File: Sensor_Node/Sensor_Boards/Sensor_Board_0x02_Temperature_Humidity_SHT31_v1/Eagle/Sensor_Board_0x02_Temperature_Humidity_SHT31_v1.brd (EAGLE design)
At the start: 55 x 35 mm, 15 parts, among them J1 M04_SMD_90, J2 M07_SMD_STRAIGHT, J4 ARDUINO_ISP, U2 ATMEGA328P_TQFP, Y1 8MHZ

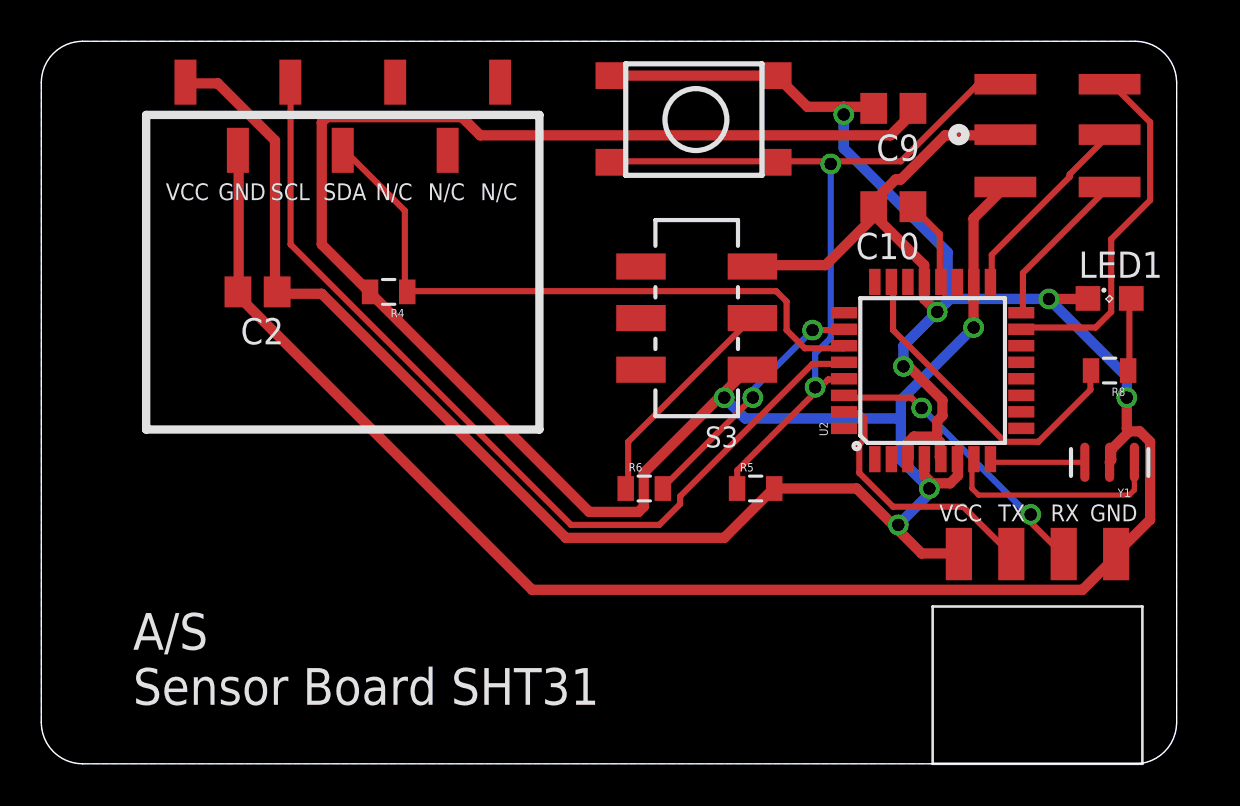
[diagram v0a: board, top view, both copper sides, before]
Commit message: Changes on SensModule SHT31
- removed R4
- added pogopin programming connector
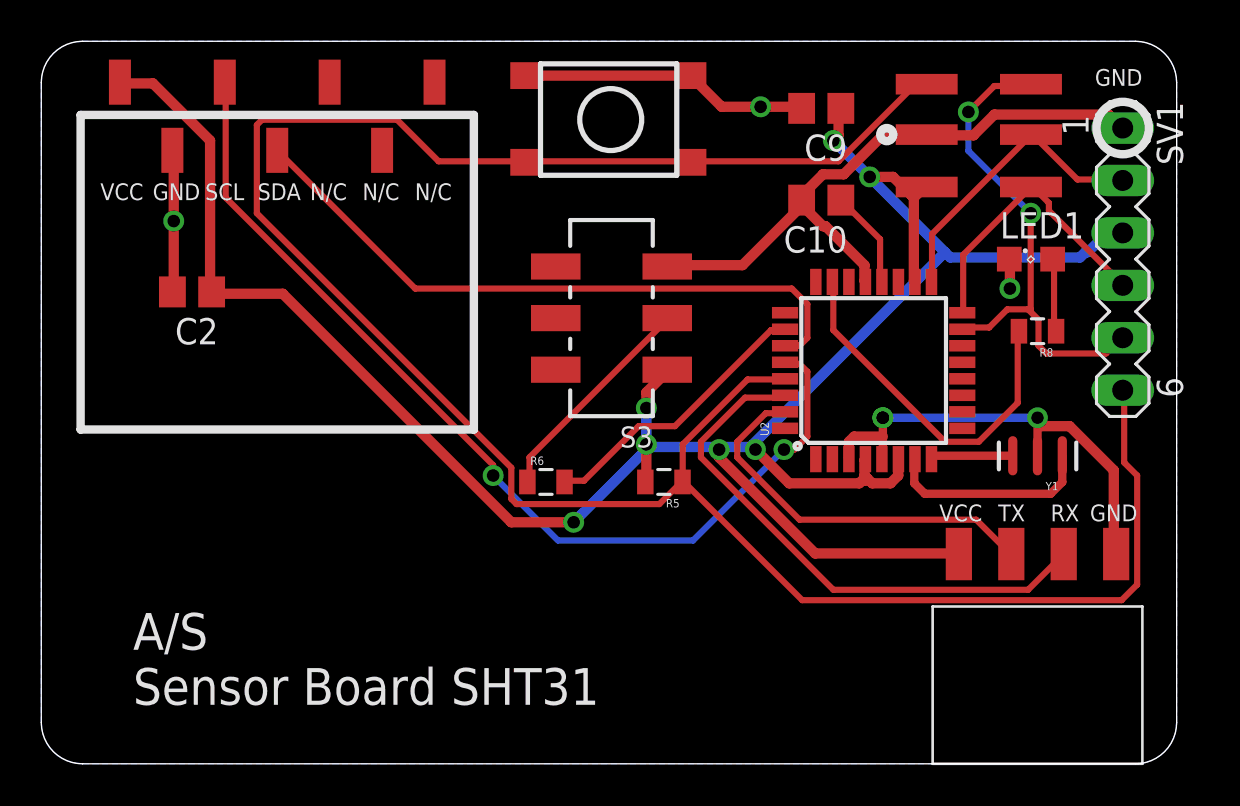
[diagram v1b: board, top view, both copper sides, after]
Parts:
- removed R4: 10k, SparkFun-Passives:0805
- added SV1: (no value), con-lstb:MA06-1
- moved R6 4.77 mm to (24.4, 13.7)
- moved R5 4.46 mm to (30.2, 13.7), turned to 180 degrees
- moved LED1 4.26 mm to (47.9, 24.4)
- moved S3 4.13 mm to (27.6, 21.6)
- moved S1 4.13 mm to (23.5, 33.3)
- moved R8 3.98 mm to (48.3, 21.0)
- moved J4 3.81 mm to (47.9, 27.9)
- moved C10 3.51 mm to (37.8, 27.3)
- moved Y1 3.51 mm to (48.3, 14.9)
- moved C9 3.49 mm to (37.8, 31.8)
- moved J2 3.18 mm to (19.1, 33.0)
- moved C2 3.17 mm to (7.30, 22.9)
- moved U2 2.86 mm to (40.3, 19.1)
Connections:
- net GND: now also SV1.1
- net MISO: now also SV1.4
- net MOSI: now also SV1.5
- net RESET: now also SV1.6
- net SCK: now also SV1.2
- net SDA: no longer R4.1
- net VCC: now also SV1.3; no longer R4.2
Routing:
- net RESET: track 40.1 -> 109.5 mm, vias 2 -> 0
- net GND: track 138.9 -> 76.3 mm, vias 5 -> 6
- net VCC: track 151.8 -> 115.5 mm, vias 4 -> 7
- net MCU_RXI: track 14.0 -> 26.7 mm, vias 2 -> 0
- net MOSI: track 17.4 -> 24.7 mm, vias 0 -> 2
- net MISO: track 7.90 -> 14.1 mm
- net MCU_TXO: track 12.8 -> 18.9 mm
- net SCK: track 9.53 -> 14.5 mm
- net SCL: track 43.8 -> 47.5 mm, vias 0 -> 2
- net L1: track 16.2 -> 17.8 mm
- net DBG_ENABLE: track 12.2 -> 13.7 mm, vias 2 -> 0
- net N$2: track 10.9 -> 10.1 mm
- net N$15: track 4.20 -> 4.80 mm
- net N$1: track 4.64 -> 4.10 mm

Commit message: Changes on all boards
- added capacitor on reset-path
- changed order of pogopin programmer pins

Pulse-Board:
- Deleted input-jumper. Currently one interrupt-pin missing, so print is
not yet routed.
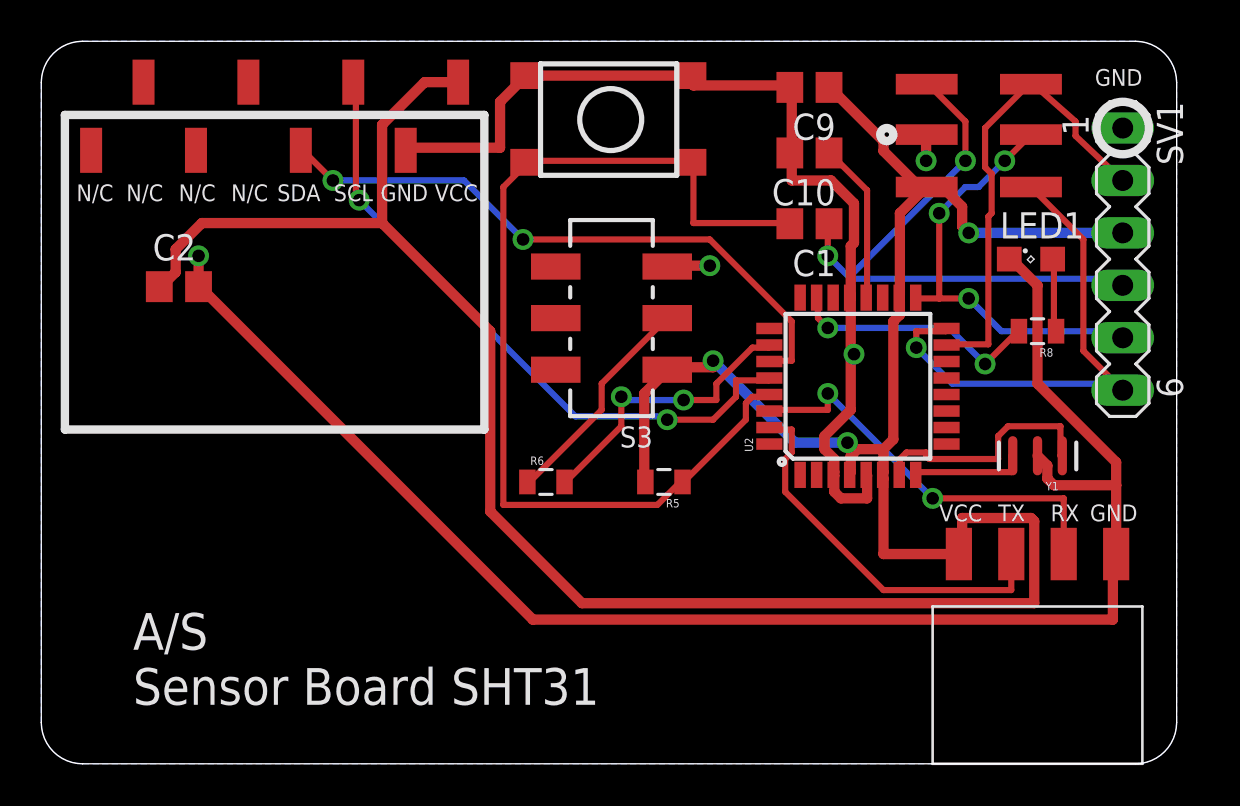
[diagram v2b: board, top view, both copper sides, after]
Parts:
- removed J2: M07_SMD_STRAIGHT, myownthings:M07_SMD_STRAIGHT
- added C1: 100n, eagle-ltspice:C0805
- added U$20: M08_SMD_STRAIGHT, myownthings:M08_SMD_STRAIGHT
- moved C10 2.36 mm to (37.2, 29.6)
- moved C9 1.17 mm to (37.2, 32.8)
- moved U2 1.08 mm to (39.6, 18.3)
- moved C2 0.68 mm to (6.67, 23.1), turned to 0 degrees
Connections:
- new net N$4: C1.2, R5.1, S1.3, S1.4, U2.29
- net GND: now also U$20.P7; no longer J2.P6
- net MISO: now also SV1.6; no longer SV1.4
- net MOSI: now also SV1.2; no longer SV1.5
- net RESET: now also C1.1, SV1.4; no longer R5.1, S1.3, S1.4, SV1.6, U2.29
- net SCK: now also SV1.5; no longer SV1.2
- net SCL: now also U$20.P6; no longer J2.P5
- net SDA: now also U$20.P5; no longer J2.P4
- net VCC: now also U$20.P8; no longer J2.P7
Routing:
- net RESET: track 109.5 -> 28.9 mm, vias 0 -> 2
- net GND: track 76.3 -> 128.1 mm, vias 6 -> 4
- net N$4: track 0.00 -> 48.4 mm
- net VCC: track 115.5 -> 135.9 mm, vias 7 -> 3
- net SCL: track 47.5 -> 31.5 mm
- net MISO: track 14.1 -> 24.9 mm, vias 0 -> 1
- net MCU_RXI: track 26.7 -> 19.9 mm, vias 0 -> 2
- net SCK: track 14.5 -> 21.0 mm, vias 0 -> 3
- net L1: track 17.8 -> 12.3 mm, vias 0 -> 2
- net N$15: track 4.80 -> 7.79 mm
- net MOSI: track 24.7 -> 22.7 mm, vias 2 -> 0
- net N$2: track 10.1 -> 11.7 mm
- net N$1: track 4.10 -> 5.60 mm
- net SDA: track 31.6 -> 30.2 mm, vias 0 -> 2
- net DBG_ENABLE: track 13.7 -> 14.2 mm, vias 0 -> 2

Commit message: Changed SensorBoard SHT31
- changed pogopin-programmer to FTDI
- connection with comboard is now over software serial instead of
hardware serial
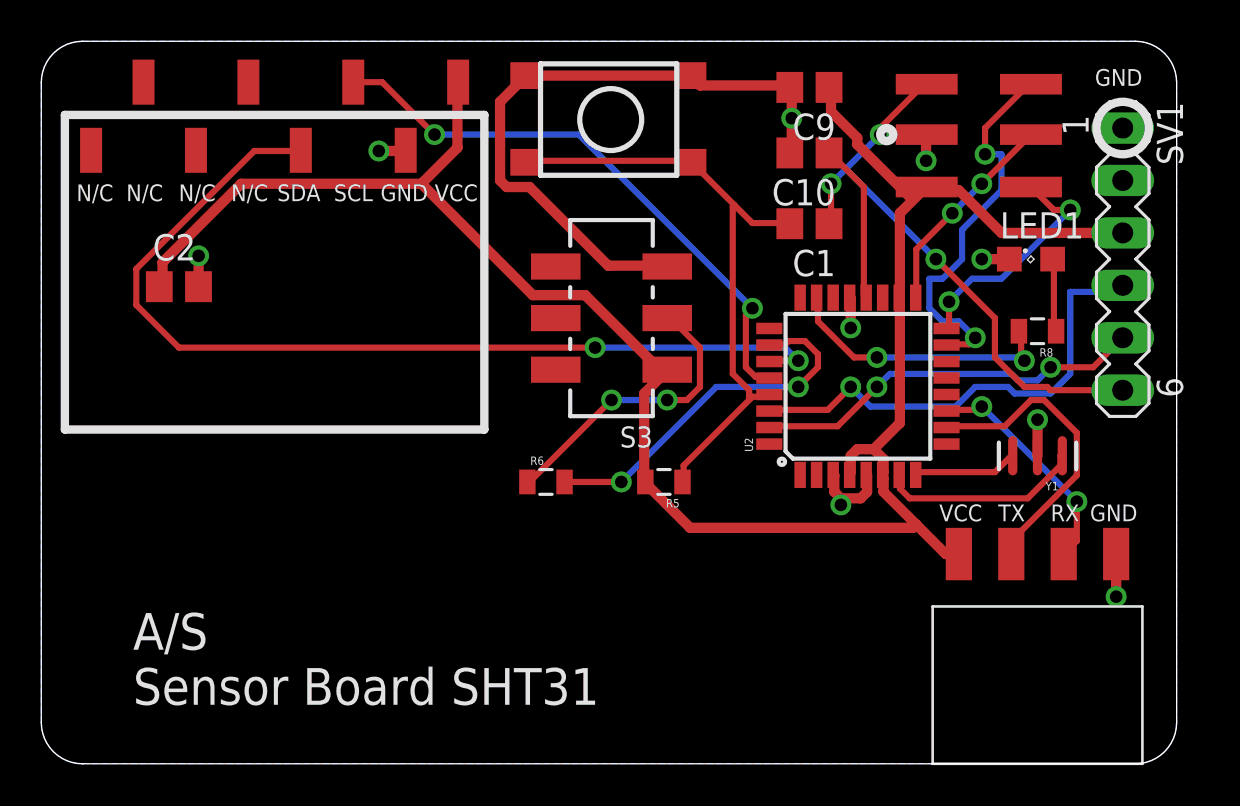
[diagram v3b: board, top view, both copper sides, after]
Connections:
- new net FTDI_RXI: SV1.4, U2.30
- new net FTDI_TXO: SV1.5, U2.31
- net GND: now also SV1.2
- net MCU_RXI: now also U2.11; no longer U2.30
- net MCU_TXO: now also U2.10; no longer U2.31
- net MISO: no longer SV1.6
- net MOSI: no longer SV1.2
- net RESET: now also SV1.6; no longer SV1.4
- net SCK: no longer SV1.5
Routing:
- net GND: track 128.1 -> 46.3 mm, vias 4 -> 9
- net VCC: track 135.9 -> 98.3 mm, vias 3 -> 0
- net FTDI_RXI: track 0.00 -> 23.0 mm, vias 0 -> 1
- net FTDI_TXO: track 0.00 -> 19.2 mm, vias 0 -> 2
- net N$4: track 48.4 -> 30.3 mm
- net SDA: track 30.2 -> 46.7 mm
- net MISO: track 24.9 -> 11.5 mm, vias 1 -> 2
- net SCK: track 21.0 -> 10.2 mm, vias 3 -> 2
- net MCU_RXI: track 19.9 -> 11.1 mm
- net MCU_TXO: track 18.9 -> 14.7 mm
- net DBG_ENABLE: track 14.2 -> 17.9 mm
- net MOSI: track 22.7 -> 18.9 mm, vias 0 -> 2
- net N$3: track 10.8 -> 14.4 mm, vias 0 -> 2
- net SCL: track 31.5 -> 28.2 mm
- net N$2: track 11.7 -> 9.87 mm
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
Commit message: Changed some SensorBoards
SHT31
- new routing

PULSE
- pogopin programmer now over FTDI
- interrupt to comboard now comes from atmega

TSL2561
- pogopin programmer now over FTDI

PROTOYPING
- changed title of schematic
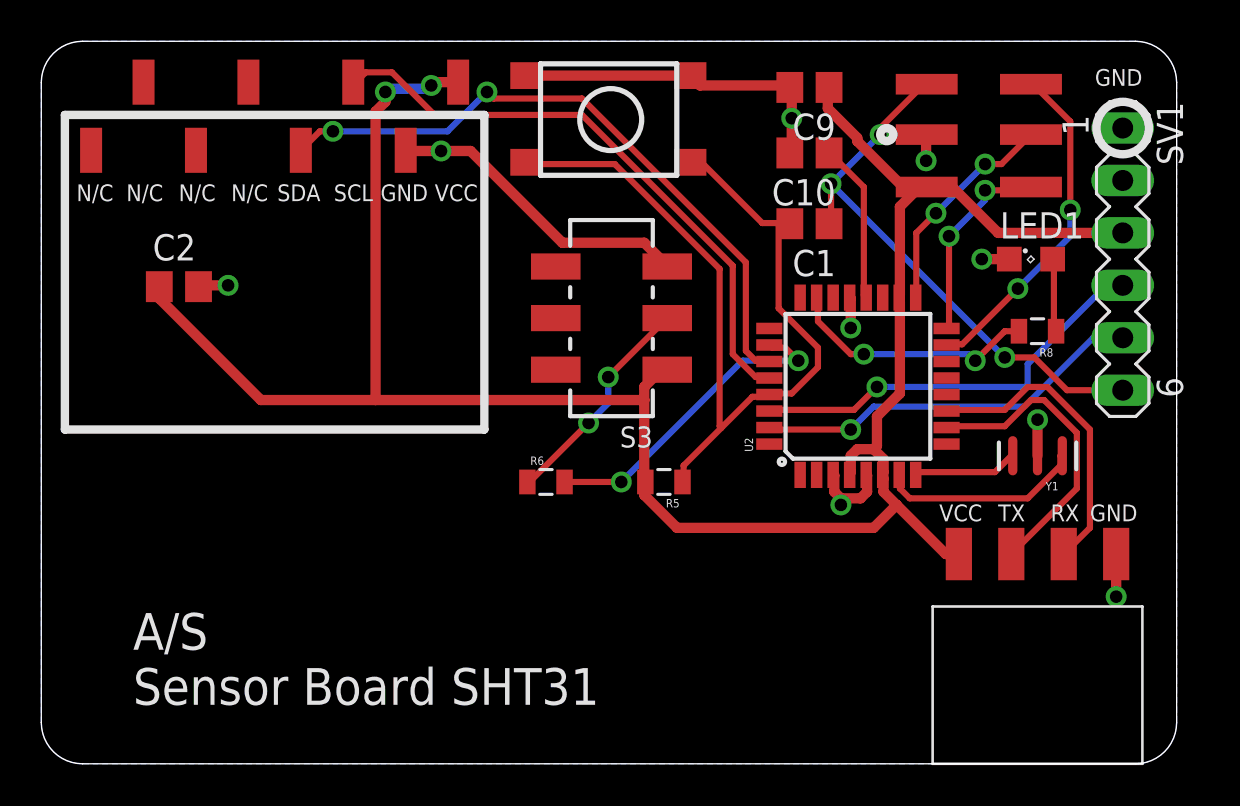
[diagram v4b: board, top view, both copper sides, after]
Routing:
- net SDA: track 46.7 -> 31.8 mm
- net N$4: track 30.3 -> 43.0 mm
- net VCC: track 98.3 -> 106.6 mm, vias 0 -> 2
- net MCU_RXI: track 11.1 -> 14.8 mm, vias 2 -> 0
- net N$3: track 14.4 -> 10.8 mm
- net FTDI_RXI: track 23.0 -> 20.3 mm
- net DBG_ENABLE: track 17.9 -> 15.5 mm
- net MOSI: track 18.9 -> 16.5 mm
- net GND: track 46.3 -> 44.6 mm
- net MISO: track 11.5 -> 9.80 mm
- net L1: track 13.6 -> 12.3 mm
- net SCL: track 28.2 -> 29.0 mm, vias 2 -> 0
- net RESET: track 27.9 -> 27.3 mm
- net FTDI_TXO: track 19.2 -> 19.0 mm, vias 2 -> 1

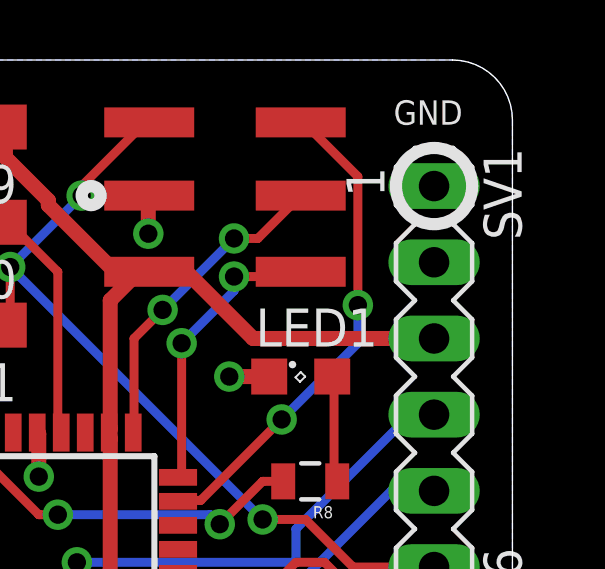
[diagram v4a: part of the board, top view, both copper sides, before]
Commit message: Finished some boards.
- Minor changes on all boards except
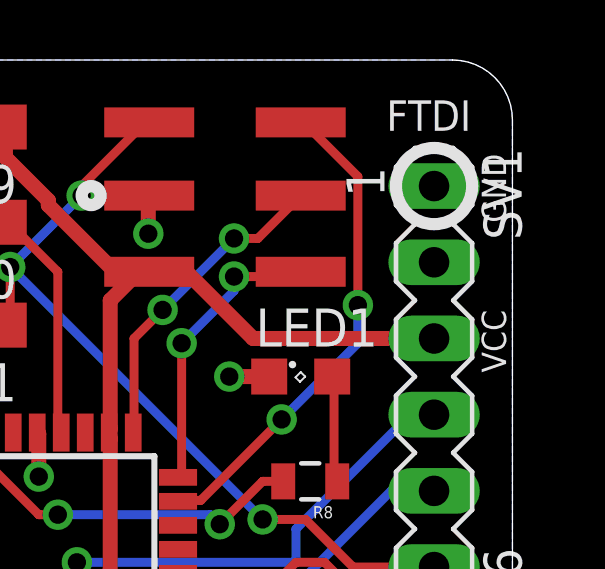
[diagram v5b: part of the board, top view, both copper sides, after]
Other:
- board text added: "FTDI"
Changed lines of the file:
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@@
 Sensor Board SHT31</text>
 <circle x="40.9575" y="30.48" radius="0.3175" width="0.4064" layer="21"/>
-<text x="53.34" y="33.655" size="0.8128" layer="21" rot="R180">GND</text>
 <circle x="52.3875" y="30.7975" radius="1.27" width="0.4064" layer="21"/>
 <text x="3.4925" y="28.067" size="0.8128" layer="21" rot="R180">N/C</text>
+<text x="53.975" y="26.67" size="0.8128" layer="21" rot="R270">VCC</text>
+<text x="50.8" y="32.639" size="1.016" layer="21">FTDI</text>
+<text x="53.975" y="31.877" size="0.8128" layer="21" rot="R270">GND</text>
 </plain>
 <attributes>
